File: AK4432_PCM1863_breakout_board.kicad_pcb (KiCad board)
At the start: 2 copper layers, 24 parts, among them J1 Conn_01x08_Pin, U1 PCM1863DBTR, U2 AK4432VT, U2 LD1117S33TR_SOT223, U3 AK4432VT, U4 SN74AVC1T45DCKR, Y1 ECS-2520MV-xxx-xx

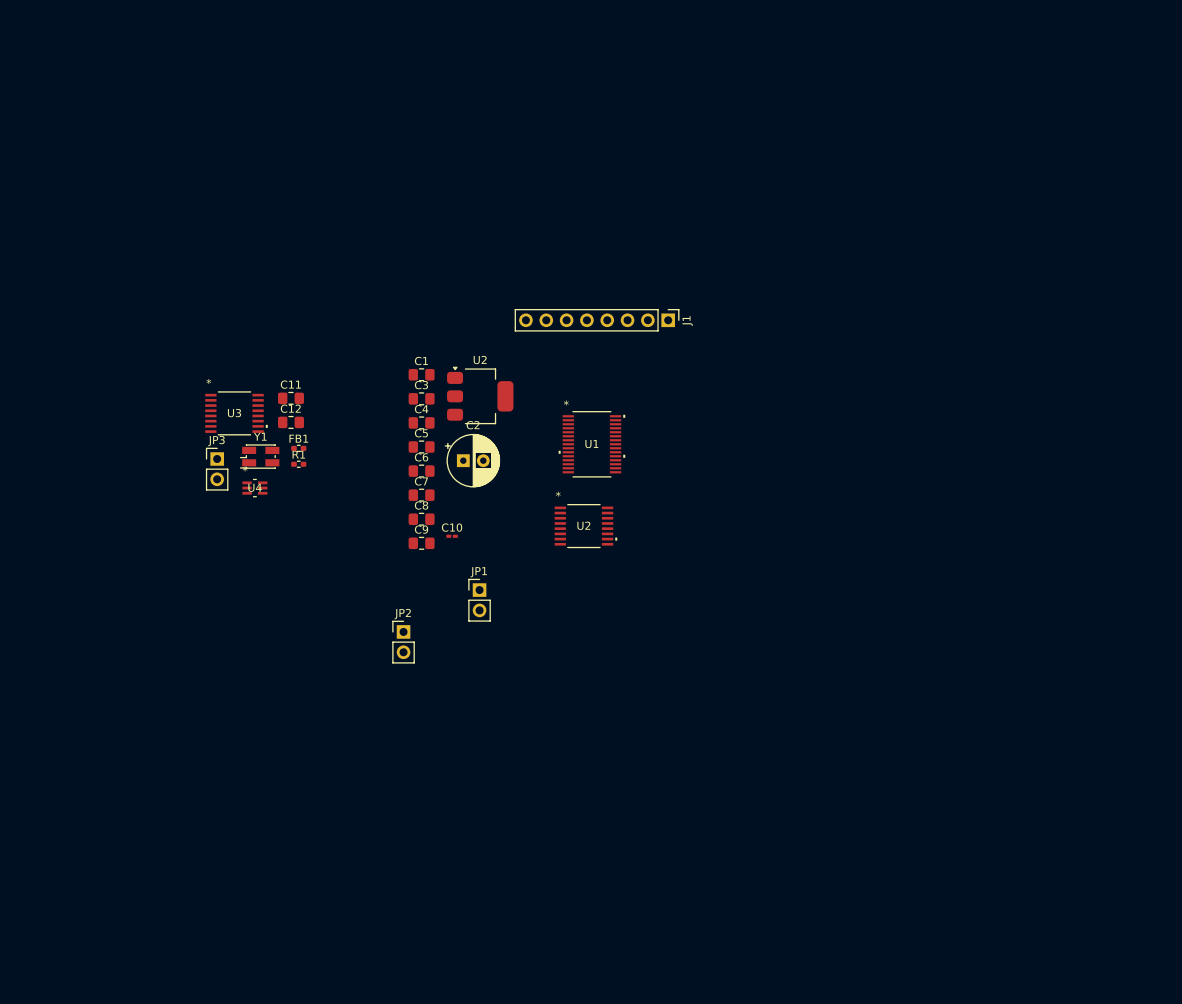
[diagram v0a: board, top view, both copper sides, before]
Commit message: finished preliminary schematic, started laying out.
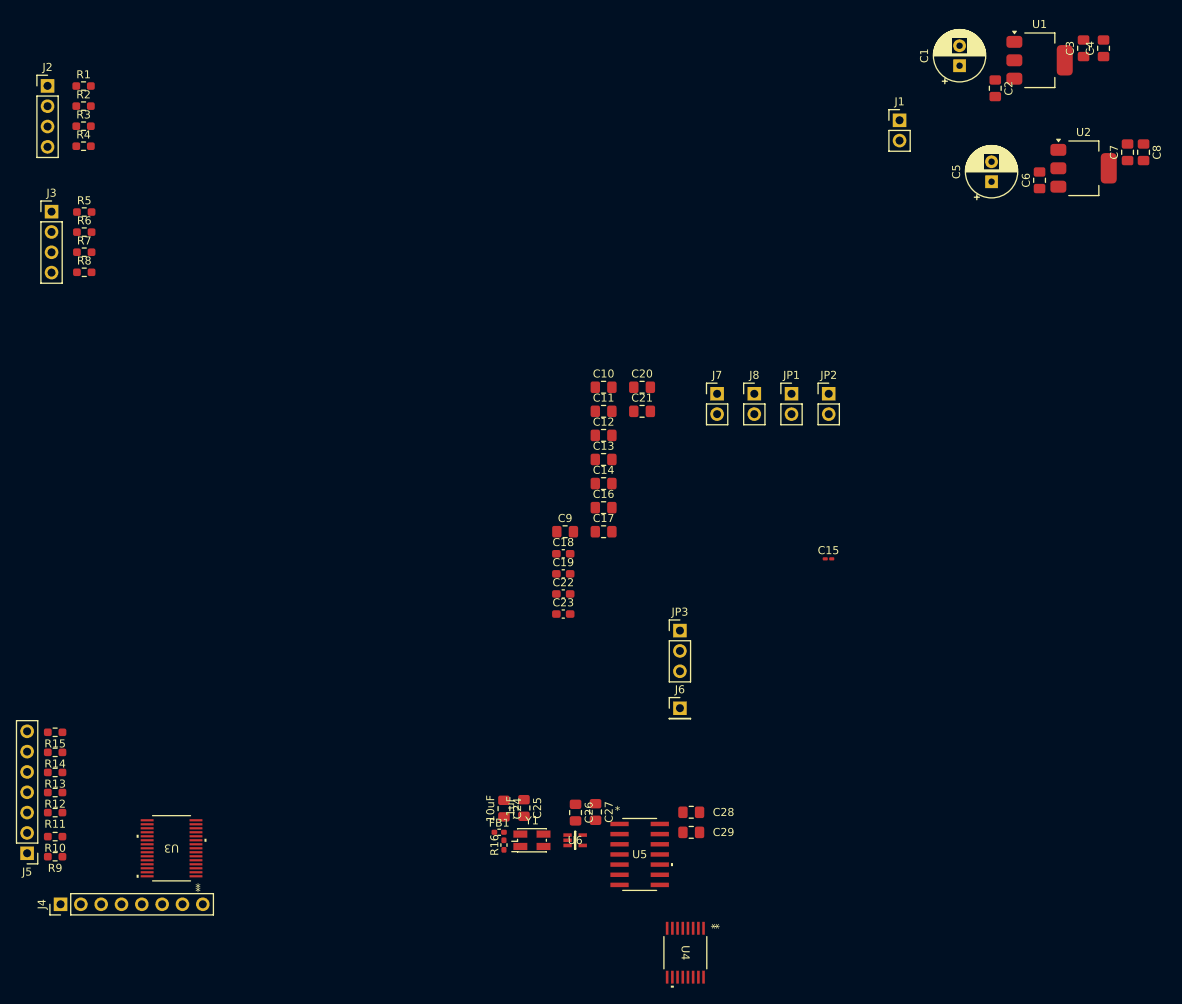
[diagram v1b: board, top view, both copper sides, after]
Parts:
- removed the U2 at (115.6, 84.0)
- removed the U2 at (128.5, 100.2)
- added C13: 10uF, Capacitor_SMD:C_0805_2012Metric_Pad1.18x1.45mm_HandSolder, F.Cu at (131.0, 91.9)
- added C14: .1uF, Capacitor_SMD:C_0805_2012Metric_Pad1.18x1.45mm_HandSolder, F.Cu at (131.0, 94.9)
- added C15: 1uF, Capacitor_SMD:C_0201_0603Metric_Pad0.64x0.40mm_HandSolder, F.Cu at (159.1, 104.3)
- added C16: 10uF, Capacitor_SMD:C_0805_2012Metric_Pad1.18x1.45mm_HandSolder, F.Cu at (131.0, 97.9)
- added C17: .1uF, Capacitor_SMD:C_0805_2012Metric_Pad1.18x1.45mm_HandSolder, F.Cu at (131.0, 100.9)
- added C18: 1uF, Capacitor_SMD:C_0603_1608Metric_Pad1.08x0.95mm_HandSolder, F.Cu at (126.0, 103.7)
- added C19: 2.2uF, Capacitor_SMD:C_0603_1608Metric_Pad1.08x0.95mm_HandSolder, F.Cu at (126.0, 106.2)
- added C20: 10uF, Capacitor_SMD:C_0805_2012Metric_Pad1.18x1.45mm_HandSolder, F.Cu at (135.8, 82.9)
- added C21: .1uF, Capacitor_SMD:C_0805_2012Metric_Pad1.18x1.45mm_HandSolder, F.Cu at (135.8, 85.9)
- added C22: 1uF, Capacitor_SMD:C_0603_1608Metric_Pad1.08x0.95mm_HandSolder, F.Cu at (126.0, 108.7)
- added C23: 1uF, Capacitor_SMD:C_0603_1608Metric_Pad1.08x0.95mm_HandSolder, F.Cu at (126.0, 111.2)
- added C24: 10uF, Capacitor_SMD:C_0805_2012Metric_Pad1.18x1.45mm_HandSolder, F.Cu at (118.5, 135.5)
- added C25: .1uF, Capacitor_SMD:C_0805_2012Metric_Pad1.18x1.45mm_HandSolder, F.Cu at (121.0, 135.5)
- added C26: .1uF, Capacitor_SMD:C_0805_2012Metric_Pad1.18x1.45mm_HandSolder, F.Cu at (127.5, 136.0)
- added C27: 10uF, Capacitor_SMD:C_0805_2012Metric_Pad1.18x1.45mm_HandSolder, F.Cu at (130.0, 136.0)
- added C28: 10uF, Capacitor_SMD:C_0805_2012Metric_Pad1.18x1.45mm_HandSolder, F.Cu at (142.0, 136.0)
- added C29: .1uF, Capacitor_SMD:C_0805_2012Metric_Pad1.18x1.45mm_HandSolder, F.Cu at (142.0, 138.5)
- added J2: Conn_01x04_Pin, Connector_PinHeader_2.54mm:PinHeader_1x04_P2.54mm_Vertical, F.Cu at (61.5, 45.2)
- added J3: Conn_01x04_Pin, Connector_PinHeader_2.54mm:PinHeader_1x04_P2.54mm_Vertical, F.Cu at (62.0, 60.9)
- added J4: Conn_01x08_Pin, Connector_PinHeader_2.54mm:PinHeader_1x08_P2.54mm_Vertical, F.Cu at (63.1, 147.5)
- added J5: Conn_01x07_Pin, Connector_PinHeader_2.54mm:PinHeader_1x07_P2.54mm_Vertical, F.Cu at (58.9, 141.1)
- added J6: Conn_01x01_Pin, Connector_PinHeader_2.54mm:PinHeader_1x01_P2.54mm_Vertical, F.Cu at (140.5, 123.0)
- added J7: Conn_01x02_Pin, Connector_PinHeader_2.54mm:PinHeader_1x02_P2.54mm_Vertical, F.Cu at (145.2, 83.7)
- added J8: Conn_01x02_Pin, Connector_PinHeader_2.54mm:PinHeader_1x02_P2.54mm_Vertical, F.Cu at (149.8, 83.7)
- added R10: 100, Resistor_SMD:R_0603_1608Metric_Pad0.98x0.95mm_HandSolder, F.Cu at (62.4, 139.0)
- added R11: 100, Resistor_SMD:R_0603_1608Metric_Pad0.98x0.95mm_HandSolder, F.Cu at (62.4, 136.0)
- added R12: 100, Resistor_SMD:R_0603_1608Metric_Pad0.98x0.95mm_HandSolder, F.Cu at (62.4, 133.5)
- added R13: 100, Resistor_SMD:R_0603_1608Metric_Pad0.98x0.95mm_HandSolder, F.Cu at (62.4, 131.0)
- added R14: 100, Resistor_SMD:R_0603_1608Metric_Pad0.98x0.95mm_HandSolder, F.Cu at (62.4, 128.5)
- added R15: 100, Resistor_SMD:R_0603_1608Metric_Pad0.98x0.95mm_HandSolder, F.Cu at (62.4, 126.0)
- added R16: 10k, Resistor_SMD:R_0402_1005Metric_Pad0.72x0.64mm_HandSolder, F.Cu at (118.5, 140.1)
- added R2: 100, Resistor_SMD:R_0603_1608Metric_Pad0.98x0.95mm_HandSolder, F.Cu at (66.0, 47.7)
- added R3: 100, Resistor_SMD:R_0603_1608Metric_Pad0.98x0.95mm_HandSolder, F.Cu at (66.0, 50.2)
- added R4: 100, Resistor_SMD:R_0603_1608Metric_Pad0.98x0.95mm_HandSolder, F.Cu at (66.0, 52.7)
- added R5: 100, Resistor_SMD:R_0603_1608Metric_Pad0.98x0.95mm_HandSolder, F.Cu at (66.1, 61.0)
- added R6: 100, Resistor_SMD:R_0603_1608Metric_Pad0.98x0.95mm_HandSolder, F.Cu at (66.1, 63.5)
- added R7: 100, Resistor_SMD:R_0603_1608Metric_Pad0.98x0.95mm_HandSolder, F.Cu at (66.1, 66.0)
- added R8: 100, Resistor_SMD:R_0603_1608Metric_Pad0.98x0.95mm_HandSolder, F.Cu at (66.1, 68.5)
- added R9: 100, Resistor_SMD:R_0603_1608Metric_Pad0.98x0.95mm_HandSolder, F.Cu at (62.4, 141.6)
- added U2: LD1117S33TR_SOT223, Package_TO_SOT_SMD:SOT-223-3_TabPin2, F.Cu at (191.0, 55.5)
- added U5: SN74HC74DR, footprints:D14-M, F.Cu at (135.5, 141.3)
- added U6: SN74LVC1G04DCKR, footprints:DCK0005A_M, F.Cu at (127.4, 139.5)
- C1: value 10uF -> 100uF; footprint Capacitor_SMD:C_0805_2012Metric_Pad1.18x1.45mm_HandSolder -> Capacitor_THT:CP_Radial_D6.3mm_P2.50mm
- C10: value 1uF -> .1uF; footprint Capacitor_SMD:C_0201_0603Metric_Pad0.64x0.40mm_HandSolder -> Capacitor_SMD:C_0805_2012Metric_Pad1.18x1.45mm_HandSolder
- C2: value 100uF -> .1uF; footprint Capacitor_THT:CP_Radial_D6.3mm_P2.50mm -> Capacitor_SMD:C_0805_2012Metric_Pad1.18x1.45mm_HandSolder
- C5: value .1uF -> 100uF; footprint Capacitor_SMD:C_0805_2012Metric_Pad1.18x1.45mm_HandSolder -> Capacitor_THT:CP_Radial_D6.3mm_P2.50mm
- C6, C8: value 10uF -> .1uF
- C7, C9: value .1uF -> 10uF
- J1: value Conn_01x08_Pin -> Conn_01x02_Pin; footprint Connector_PinHeader_2.54mm:PinHeader_1x08_P2.54mm_Vertical -> Connector_PinHeader_2.54mm:PinHeader_1x02_P2.54mm_Vertical
- JP3: value Jumper_2_Bridged -> Jumper_3_Bridged12; footprint Connector_PinHeader_2.54mm:PinHeader_1x02_P2.54mm_Vertical -> Connector_PinHeader_2.54mm:PinHeader_1x03_P2.54mm_Vertical
- R1: value 10k -> 100; footprint Resistor_SMD:R_0402_1005Metric_Pad0.72x0.64mm_HandSolder -> Resistor_SMD:R_0603_1608Metric_Pad0.98x0.95mm_HandSolder
- U1: value PCM1863DBTR -> LD1117S33TR_SOT223; footprint footprints:DBT30_TEX -> Package_TO_SOT_SMD:SOT-223-3_TabPin2
- U3: value AK4432VT -> PCM1863DBTR; footprint footprints:TSSOP16_AKM -> footprints:DBT30_TEX-M
- U4: value SN74AVC1T45DCKR -> AK4432VT; footprint footprints:DCK6 -> footprints:TSSOP16_AKM-M
- Y1: value ECS-2520MV-xxx-xx -> ECS-3225MV-491.52
- moved C8 101.2 mm to (198.5, 53.5), turned to -90 degrees
- moved C7 98.1 mm to (196.5, 53.5), turned to 90 degrees
- moved C4 97.3 mm to (193.5, 40.5), turned to 90 degrees
- moved C3 93.6 mm to (191.0, 40.5), turned to 90 degrees
- moved C6 85.4 mm to (185.5, 57.0), turned to 90 degrees
- moved C2 81.2 mm to (180.0, 45.5), turned to -90 degrees
- moved U4 79.2 mm to (141.2, 153.6), turned to -90 degrees
- moved C5 78.6 mm to (179.5, 57.2), turned to 90 degrees
- moved C1 77.5 mm to (175.5, 42.7), turned to 90 degrees
- moved U1 73.7 mm to (185.5, 42.0)
- moved JP3 61.7 mm to (140.5, 113.3)
- moved JP2 60.9 mm to (159.1, 83.7)
- moved Y1 58.7 mm to (122.0, 139.5)
- moved U3 54.9 mm to (77.0, 140.5), turned to 180 degrees
- moved R1 54.4 mm to (66.0, 45.2)
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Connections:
- C1 pad 1: /+3.3_analog -> +5V
- C10 pad 1: /VREF -> /+3.3_analog
- C11 pad 1: GND -> /LDO
- C11 pad 2: /+3.3_digital -> GND
- C12 pad 1: GND -> /LDO
- C12 pad 2: Net-(Y1-VDD) -> GND
- C5 pad 1: /+3.3_analog -> +5V
- C6 pad 1: /LDO -> +5V
- C7 pad 1: /LDO -> /+3.3_digital
- C9 pad 1: /+3.3_digital -> /+3.3_analog
- J1 pad 1: /L4/4M -> +5V
- J1 pad 2: /R4/3M -> GND
- JP1 pad 1: /GPIO3/INTC -> Net-(JP1-A)
- JP2 pad 1: Net-(JP2-A) -> /AK_PDN/RST
- JP3 pad 1: Net-(JP3-A) -> GND
- JP3 pad 2: GND -> /AK_CS/I2CFIL
- R1 pad 1: /+3.3_digital -> Net-(J2-Pin_1)
- R1 pad 2: Net-(Y1-Tri-State) -> /AK_PDN/RST
- U1 pad 1: /L2/1M -> GND
- U1 pad 2: /R2/2M -> /+3.3_analog
- U1 pad 3: /L1/1P -> +5V
- U3 pad 1: unconnected-(U3-MCLK-Pad1) -> /L2/1M
- U3 pad 11: unconnected-(U3-AOUTL-Pad11) -> /LDO
- U3 pad 12: unconnected-(U3-VCOM-Pad12) -> GND
- U3 pad 13: unconnected-(U3-VSS-Pad13) -> /+3.3_digital
- U3 pad 14: unconnected-(U3-AVDD-Pad14) -> /+3.3_digital
- U3 pad 15: unconnected-(U3-LVDD-Pad15) -> /SCKI
- U3 pad 16: unconnected-(U3-LDOO-Pad16) -> /I2S_LRCK
- U3 pad 2: unconnected-(U3-BICK-Pad2) -> /R2/2M
- U3 pad 3: unconnected-(U3-SDTI-Pad3) -> /L1/1P
- U3 pad 4: unconnected-(U3-LRCK-Pad4) -> /R1/2P
- U3 pad 5: /ADC_PDN/RST -> /MICBIAS
- U3 pad 6: Net-(JP3-A) -> /VREF
- U3 pad 7: /I2C_SCL -> GND
- U3 pad 8: /I2C_SDA -> /+3.3_analog
- U4 pad 1: unconnected-(U4-VCCA-Pad1) -> /MCLK_AKM
- U4 pad 2: unconnected-(U4-GND-Pad2) -> /I2S_BCK
- U4 pad 3: unconnected-(U4-A-Pad3) -> /I2S_DIN_DAC
- U4 pad 4: unconnected-(U4-B-Pad4) -> /I2S_LRCK
- U4 pad 5: unconnected-(U4-DIR-Pad5) -> /AK_PDN/RST
- U4 pad 6: unconnected-(U4-VCCB-Pad6) -> /AK_CS/I2CFIL
- Y1 pad 3: unconnected-(Y1-OUT-Pad3) -> Net-(U6-A)

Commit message: almost done laying out 2-layer prototype
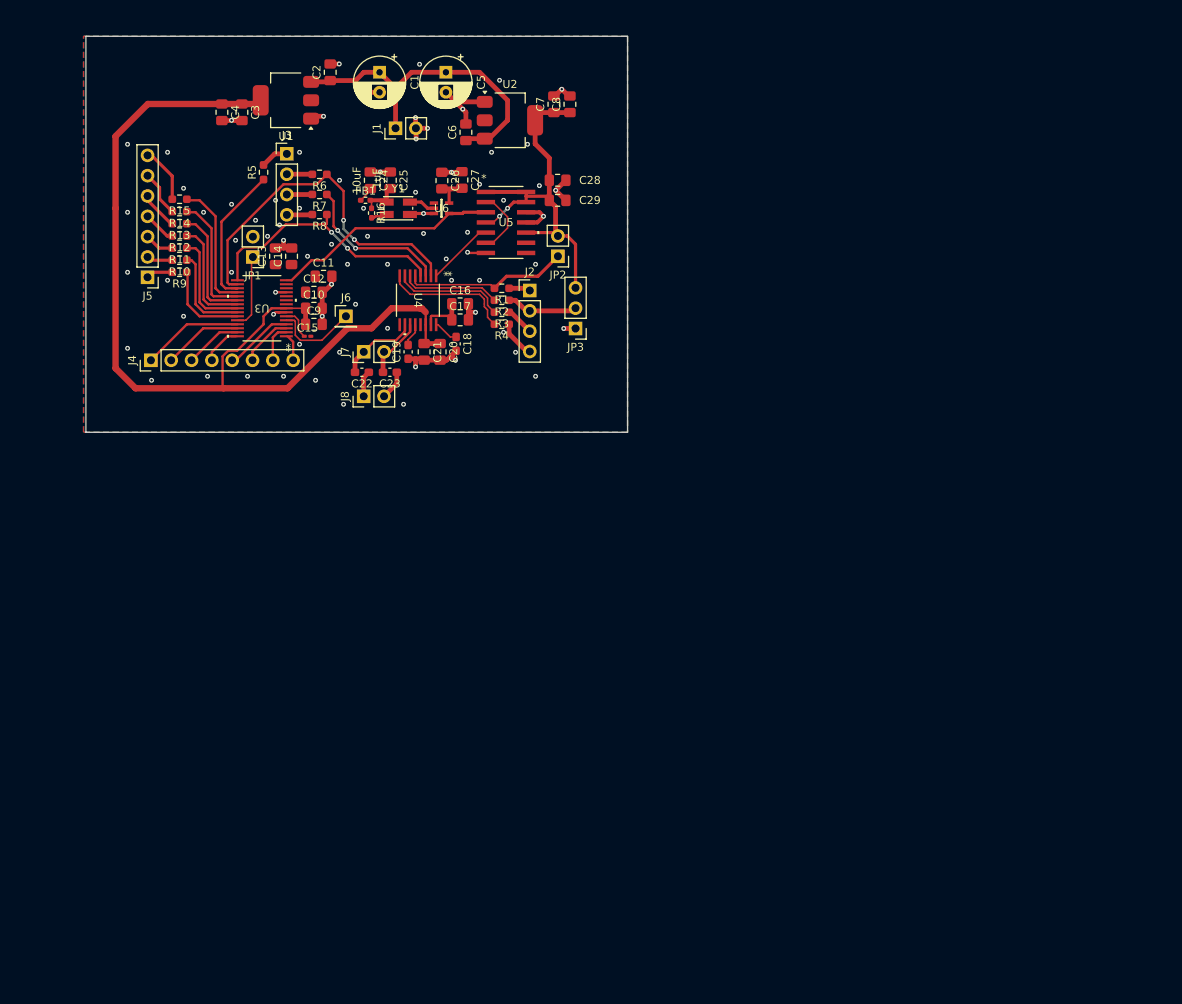
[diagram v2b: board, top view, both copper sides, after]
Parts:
- moved C4 110.5 mm to (83.3, 48.5), turned to -90 degrees
- moved C3 105.5 mm to (85.8, 48.5), turned to -90 degrees
- moved U1 94.3 mm to (91.3, 47.0), turned to 180 degrees
- moved U4 88.1 mm to (107.8, 72.0)
- moved C2 83.2 mm to (96.8, 43.5), turned to 90 degrees
- moved C26 80.7 mm to (110.8, 57.0)
- moved C27 80.7 mm to (113.3, 57.0)
- moved C28 80.7 mm to (125.3, 57.0)
- moved C29 80.7 mm to (125.3, 59.5)
- moved FB1 80.7 mm to (101.2, 59.5)
- moved U5 80.7 mm to (118.8, 62.3)
- moved U6 80.7 mm to (110.7, 60.5)
- moved Y1 80.7 mm to (105.3, 60.5)
- moved R16 80.7 mm to (102.0, 61.1), turned to -90 degrees
- moved C24 80.3 mm to (101.8, 57.0)
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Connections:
- J2 pad 2: Net-(J2-Pin_2) -> /AK_CS/I2CFIL_R
- J4 pad 5: /L2/1M -> /R1/2P
- J4 pad 6: /R2/2M -> /L1/1P
- J4 pad 7: /L1/1P -> /R2/2M
- J4 pad 8: /R1/2P -> /L2/1M
- JP3 pad 2: /AK_CS/I2CFIL -> /AK_CS/I2CFIL_R
- R2 pad 1: Net-(J2-Pin_2) -> /AK_CS/I2CFIL_R
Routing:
- net /+3.3_analog: track 0.00 -> 119.3 mm
- net GND: track 0.00 -> 67.7 mm, vias 0 -> 77
- net /+3.3_digital: track 0.00 -> 59.4 mm, vias 0 -> 2
- net /I2S_BCK: track 0.00 -> 44.4 mm, vias 0 -> 2
- net +5V: track 0.00 -> 41.9 mm
- net /I2S_LRCK: track 0.00 -> 32.5 mm, vias 0 -> 2
- net /SCKI: track 0.00 -> 28.7 mm
- net /AK_PDN/RST: track 0.00 -> 21.0 mm
- net /I2S_DIN_DAC: track 0.00 -> 19.1 mm, vias 0 -> 2
- net /I2S_DOUT_ADC: track 0.00 -> 17.7 mm
- net /GPIO3/INTC: track 0.00 -> 16.4 mm
- net /AK_SDA/CDTI: track 0.00 -> 16.0 mm
- net /GPIO2/INTB: track 0.00 -> 15.6 mm
- net /GPIO1/INTA: track 0.00 -> 14.8 mm
- net /AK_SCL/CCLK: track 0.00 -> 14.1 mm
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- added copper zone on B.Cu, net GND
- added copper zone on F.Cu, net GND
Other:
- board outline added: 67.7 x 49.5 mm

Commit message: finished 2 layer layoutgit add -A
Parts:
- moved C1 3.20 mm to (105.0, 46.0), turned to 180 degrees
- moved J1 1.57 mm to (105.5, 52.0)
- moved C11 1.00 mm to (97.0, 69.0)
- moved C5 0.38 mm to (111.5, 43.8)
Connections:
- net /L1/1P renamed /L1_1P
- net /L2/1M renamed /L2_1M
- net /L3/4P renamed /L3_4P
- net /L4/4M renamed /L4_4M
- net /R1/2P renamed /R1_2P
- net /R2/2M renamed /R2_2M
- net /R3/3P renamed /R3_3P
- net /R4/3M renamed /R4_3M
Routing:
- net /+3.3_digital: track 59.4 -> 137.3 mm, vias 2 -> 6
- net /LDO: track 0.00 -> 5.59 mm
- net GND: track 67.7 -> 64.6 mm, vias 77 -> 79
- net /I2S_LRCK: track 32.5 -> 34.9 mm
- net +5V: track 41.9 -> 43.6 mm
- net /I2S_BCK: track 44.4 -> 45.3 mm
- added copper zone on F.Cu, net /+3.3_digital
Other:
- board text added: "100Ω"
